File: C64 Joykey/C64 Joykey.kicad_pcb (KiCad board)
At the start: 2 copper layers, 99.7 x 74.9 mm, 61 parts, among them J1 Port_1, J2 Port_2, M1 Mounting, M2 Mounting, M3 Mounting, M4 Mounting, Q1 2N3904, SW1 P2_FIRE1, SW10 P1_FIRE2, SW11 P1_FIRE3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

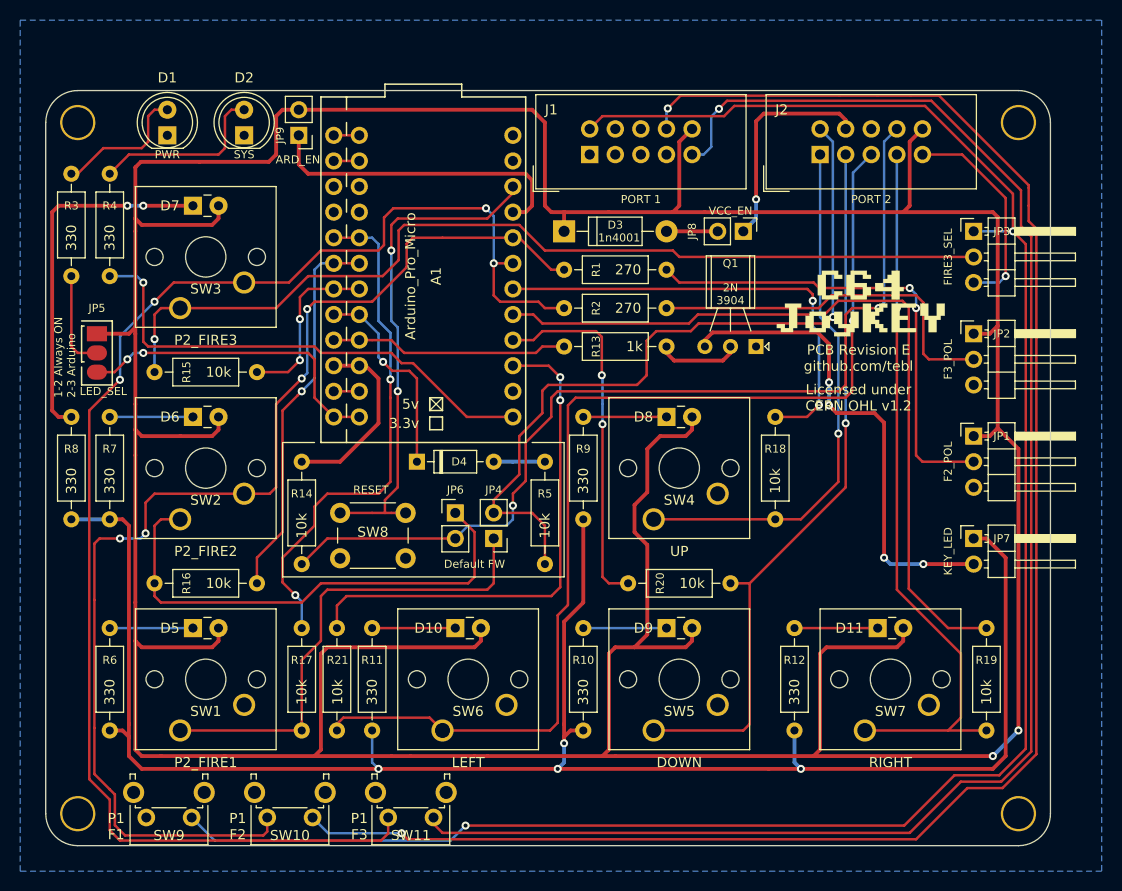
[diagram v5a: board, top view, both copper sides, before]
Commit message: Add missing CD32 button
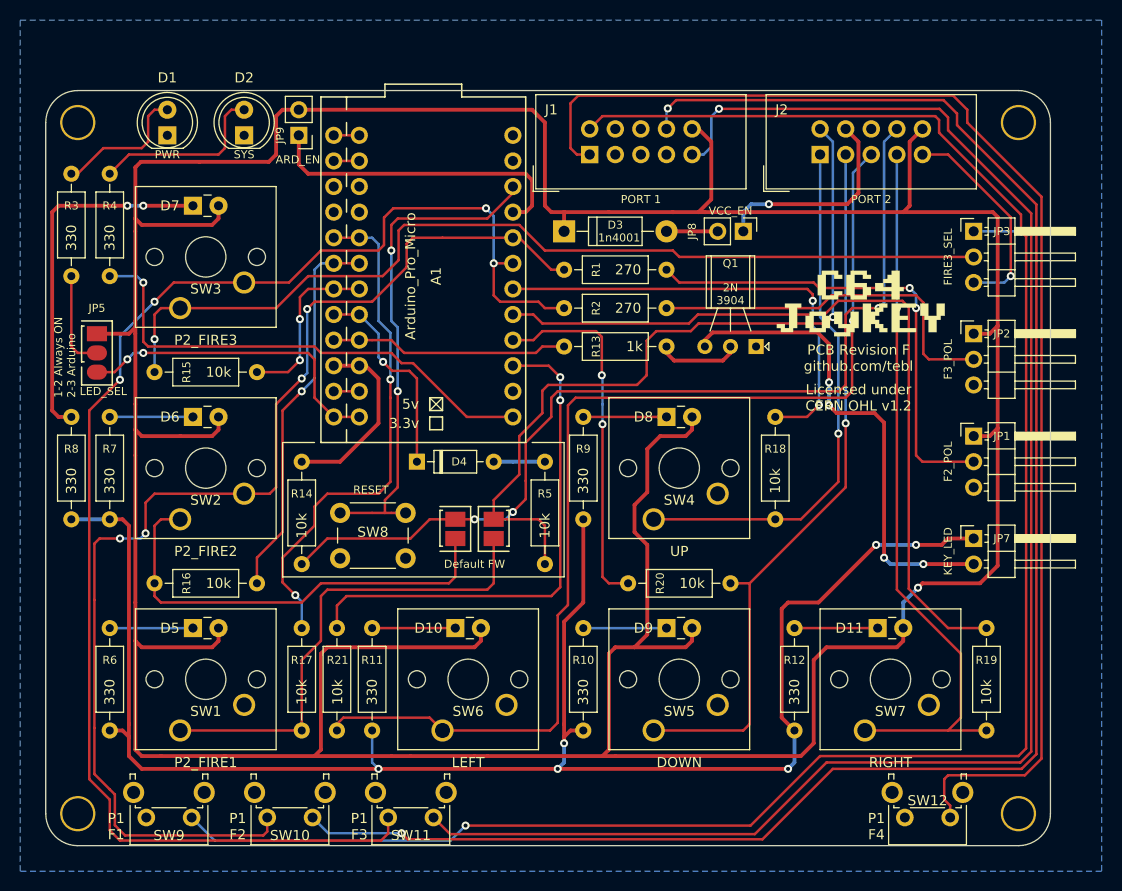
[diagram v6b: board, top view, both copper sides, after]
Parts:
- added SW12: P1_FIRE4, Button_Switch_THT:SW_Tactile_SPST_Angled_PTS645Vx31-2LFS, F.Cu at (230.7, 154.7)
- JP4: footprint Connector_PinHeader_2.54mm:PinHeader_1x02_P2.54mm_Vertical -> solder_bridge:bridge
- JP6: footprint Connector_PinHeader_2.54mm:PinHeader_1x02_P2.54mm_Vertical -> solder_bridge:bridge_r
- moved JP6 2.54 mm to (181.6, 127.0), turned to 180 degrees
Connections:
- J1 pad 1: (no net) -> P1_FIRE4
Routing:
- net P1_FIRE4: track 0.00 -> 128.9 mm
- net VCC: track 455.0 -> 430.0 mm, vias 2 -> 1
- net Net-(JP7-Pad1): track 178.8 -> 167.6 mm, vias 4 -> 6
- net Net-(JP6-Pad1): track 50.0 -> 44.8 mm
- net P1_FIRE3: track 160.1 -> 159.1 mm
- net Net-(J2-Pad7): track 21.8 -> 21.0 mm
- net P2_FIRE2: track 95.2 -> 94.8 mm, vias 2 -> 3
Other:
- board text added: "P1 F4"
- board text added: "PCB Revision F github.com/tebl"
- board text removed: "Atari_ST P1 GND GND"
- board text removed: "Default FW (FIRE1/FIRE2)"
- board text removed: "Kempston P2 GND GND"
- board text removed: "PCB Revision E github.com/tebl"

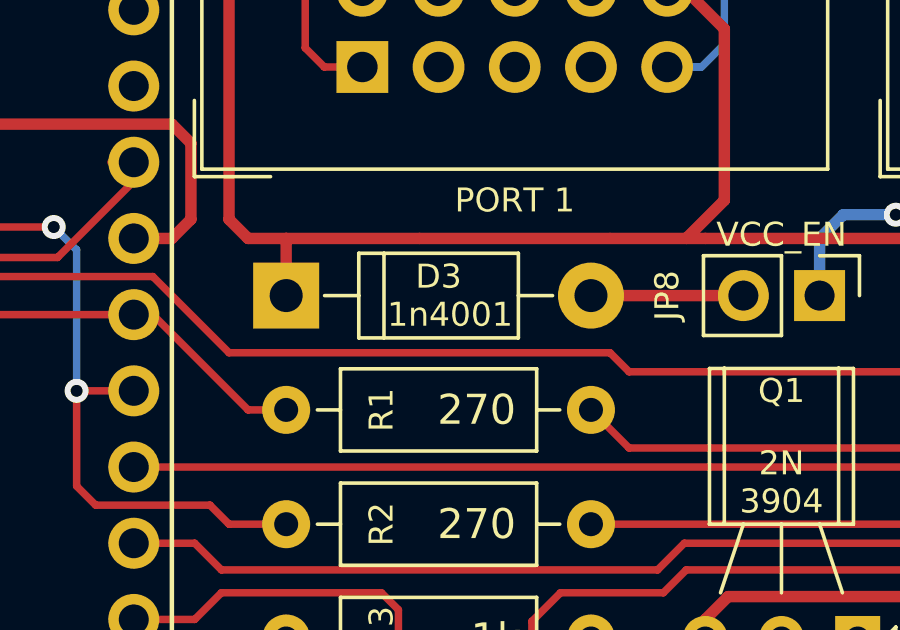
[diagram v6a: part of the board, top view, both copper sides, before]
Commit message: Change recommended diode type to 1n5819 for lower voltage drop
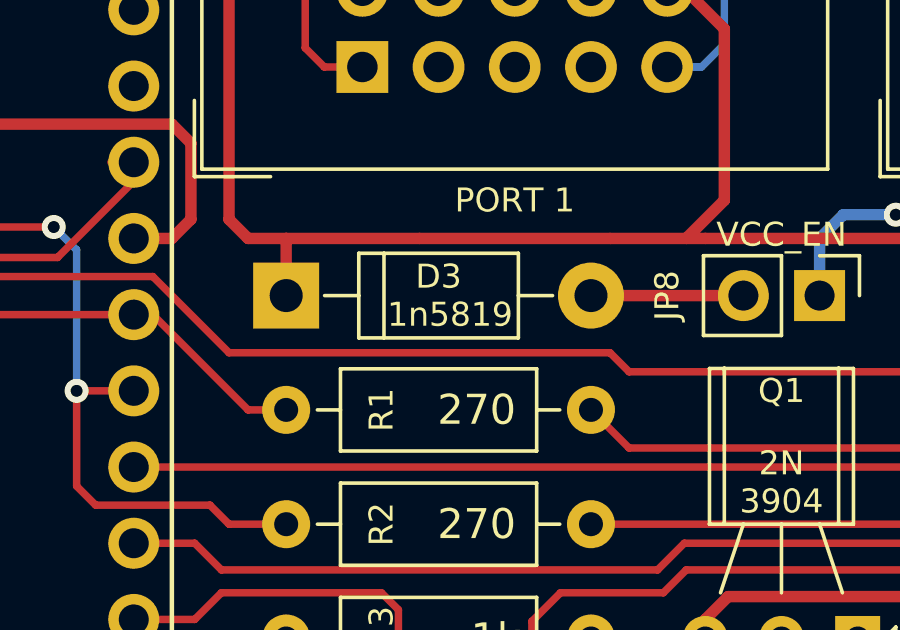
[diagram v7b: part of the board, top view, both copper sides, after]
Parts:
- D3: value 1n4001 -> 1n5819

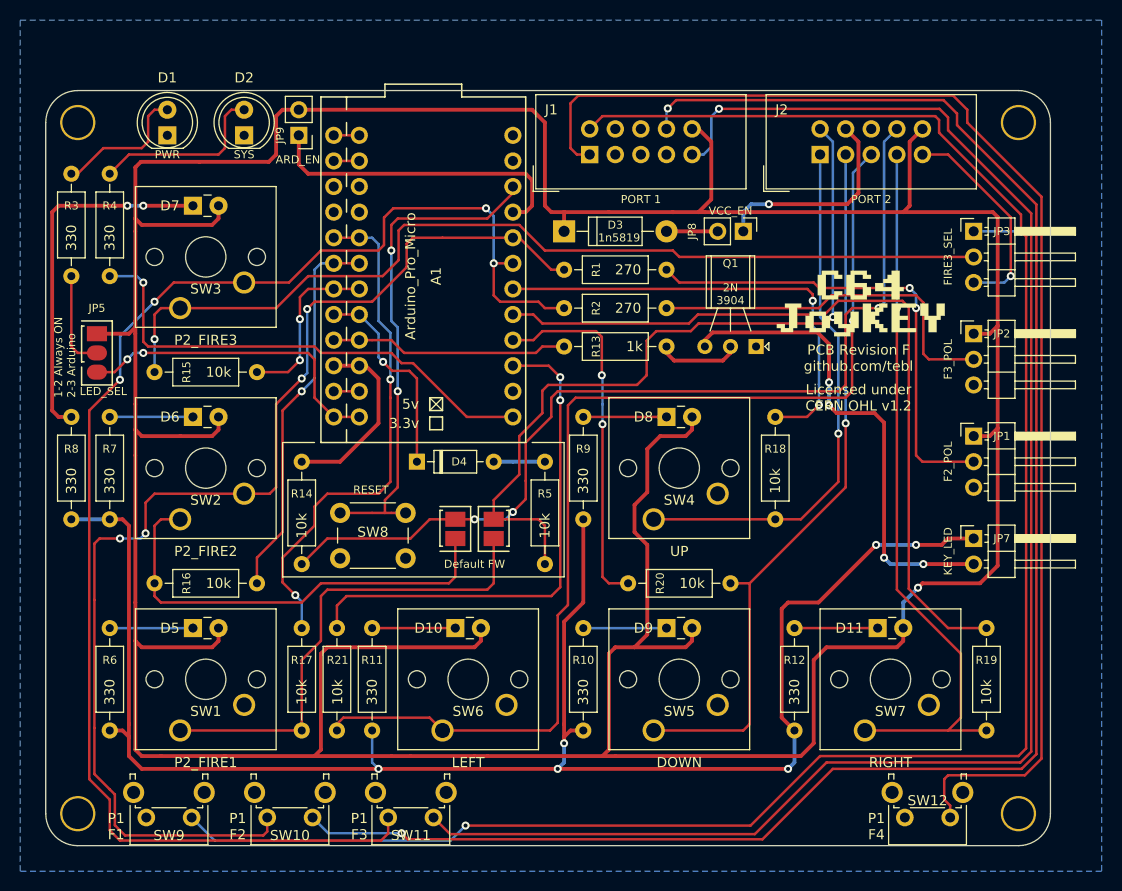
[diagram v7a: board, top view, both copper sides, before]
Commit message: Attempt update to KiCAD8
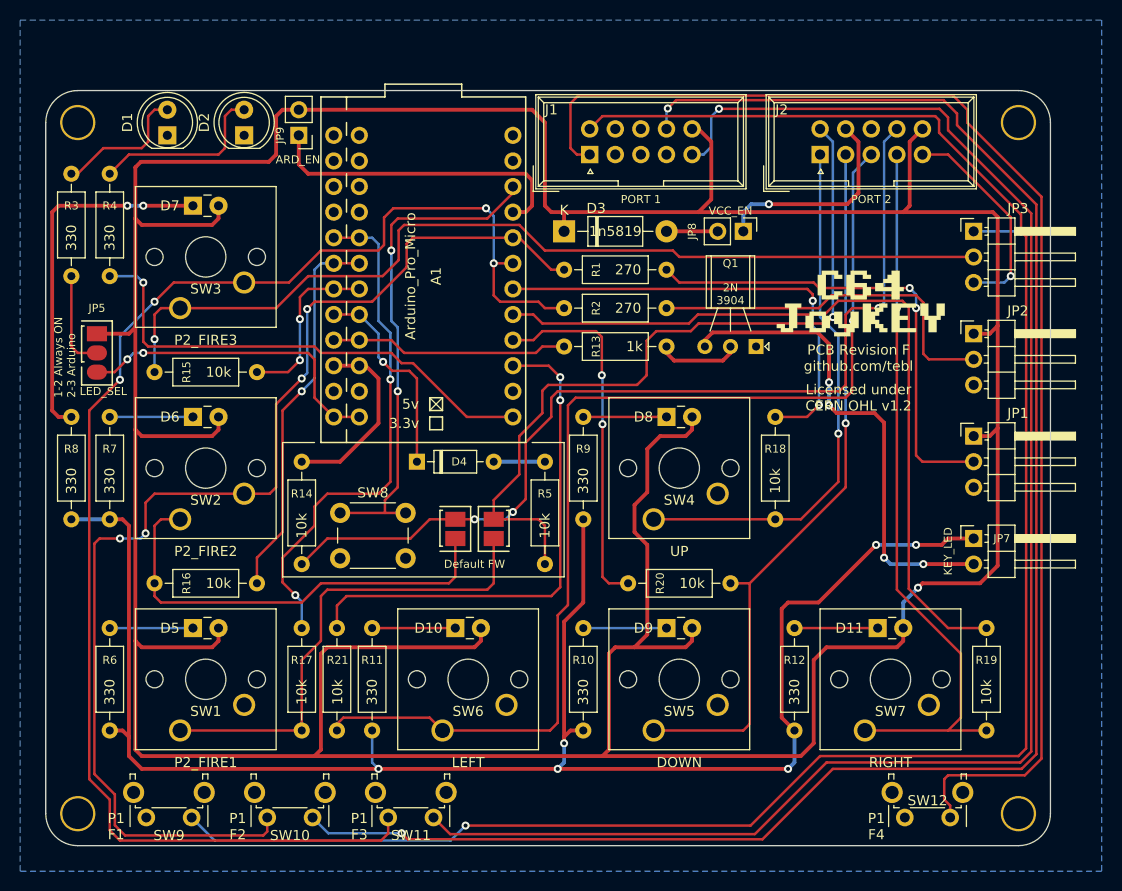
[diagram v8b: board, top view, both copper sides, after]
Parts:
- D1, D2: footprint LEDs:LED_D5.0mm -> LED_THT:LED_D5.0mm
- D3: footprint Diodes_THT:D_DO-41_SOD81_P10.16mm_Horizontal -> Diode_THT:D_DO-41_SOD81_P10.16mm_Horizontal
- JP1, JP2, JP3: footprint Pin_Headers:Pin_Header_Angled_1x03_Pitch2.54mm -> Connector_PinHeader_2.54mm:PinHeader_1x03_P2.54mm_Horizontal
- SW8: footprint Buttons_Switches_THT:SW_PUSH_6mm -> Button_Switch_THT:SW_PUSH_6mm
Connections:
- A1 pad 1: Net-(A1-Pad1) -> unconnected-(A1-TXO-Pad1)_1
- A1 pad 11: Net-(A1-Pad11) -> unconnected-(A1-D8-Pad11)_1
- A1 pad 14: (no net) -> unconnected-(A1-D16-Pad14)
- A1 pad 2: Net-(A1-Pad2) -> unconnected-(A1-RXI-Pad2)_1
- A1 pad 24: (no net) -> unconnected-(A1-RAW-Pad24)
- J1 pad 2: (no net) -> unconnected-(J1-Pin_2-Pad2)
- J1 pad 3: (no net) -> unconnected-(J1-Pin_3-Pad3)
- J1 pad 4: (no net) -> unconnected-(J1-Pin_4-Pad4)
- J1 pad 7: (no net) -> unconnected-(J1-Pin_7-Pad7)
- M1 pad 1: (no net) -> GND
- M2 pad 1: (no net) -> GND
- M3 pad 1: (no net) -> GND
- M4 pad 1: (no net) -> GND
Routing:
- net Net-(A1-Pad2): track 2.54 -> 0.00 mm
- net Net-(A1-Pad11): track 2.54 -> 0.00 mm
- net Net-(A1-Pad1): track 2.54 -> 0.00 mm
- net Net-(A1-RST): track 50.6 -> 49.2 mm
- net VCC: track 430.0 -> 428.8 mm
- net Net-(JP4-Pad1): track 49.2 -> 48.3 mm
- net P2_LEFT: track 108.6 -> 108.0 mm
- net Net-(D1-A): track 13.6 -> 13.0 mm
- net /UNDERGLOW: track 24.3 -> 23.6 mm
- net FIRE2_POL: track 118.1 -> 117.4 mm
- net /FIRE2_OUT: track 18.6 -> 18.0 mm
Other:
- net class Default removed
- net class PWR removed
- board text added: "~{IMPORTANT! Configure} FIRE2/FIRE3 polarity according to what the system required by the system, leave unjumpered (N/C) if you are not sure. You break it, you fix it!"
- board text removed: "~IMPORTANT! Configure FIRE2/FIRE3 polarity according to what the system required by the system, leave unjumpered (N/C) if you are not sure. You break it, you fix it!"
